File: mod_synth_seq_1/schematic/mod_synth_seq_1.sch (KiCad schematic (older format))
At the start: 43 parts, among them J1 CV1, J10 Reset, J11 Clock, J12 Gate Out, J2 Step 1 Gate, J3 Step 2 Gate, J4 Step 3 Gate, J5 Step 4 Gate

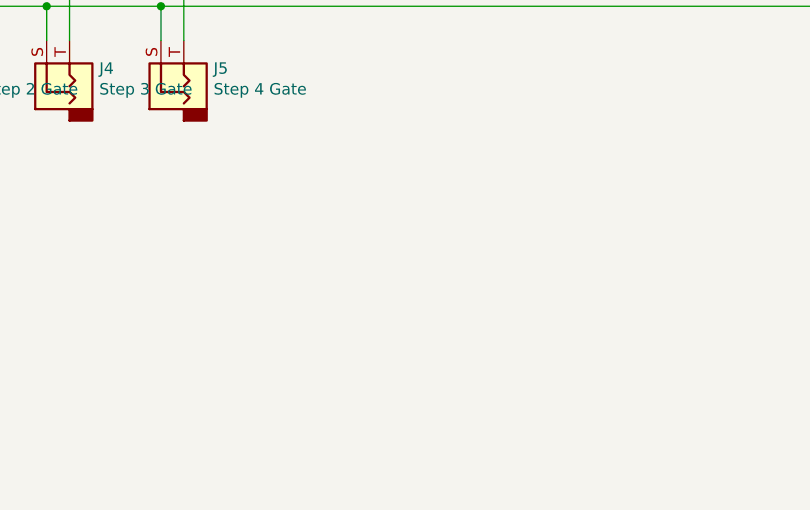
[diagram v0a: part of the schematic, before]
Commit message: Add missing connector
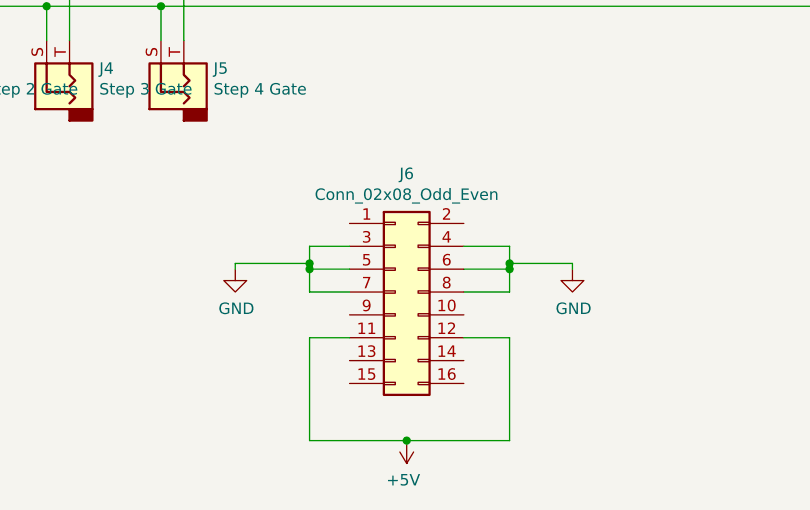
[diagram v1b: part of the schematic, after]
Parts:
- added J6: Conn_02x08_Odd_Even, Connector_IDC:IDC-Header_2x08_P2.54mm_Vertical, symbol Connector_Generic:Conn_02x08_Odd_Even
- R2, R20, R21, R4, R6, R8: footprint Resistor_THT:R_Axial_DIN0207_L6.3mm_D2.5mm_P10.16mm_Horizontal -> Resistor_THT:R_Axial_DIN0207_L6.3mm_D2.5mm_P2.54mm_Vertical
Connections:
- net +5V: now also J6.11 (Pin_11), J6.12 (Pin_12)
- net GND: now also J6.3 (Pin_3), J6.4 (Pin_4), J6.5 (Pin_5), J6.6 (Pin_6), J6.7 (Pin_7), J6.8 (Pin_8)
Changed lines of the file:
@@
 EESchema Schematic File Version 4
+LIBS:mod_synth_seq_1-cache
 EELAYER 29 0
 EELAYER END
@@
 F 0 "R2" H 2770 1546 50  0000 L CNN
 F 1 "1k" H 2770 1455 50  0000 L CNN
-F 2 "Resistor_THT:R_Axial_DIN0207_L6.3mm_D2.5mm_P10.16mm_Horizontal" V 2630 1500 50  0001 C CNN
+F 2 "Resistor_THT:R_Axial_DIN0207_L6.3mm_D2.5mm_P2.54mm_Vertical" V 2630 1500 50  0001 C CNN
 F 3 "~" H 2700 1500 50  0001 C CNN
 	1    2700 1500
@@
 F 0 "R4" H 3270 1546 50  0000 L CNN
 F 1 "1k" H 3270 1455 50  0000 L CNN
-F 2 "Resistor_THT:R_Axial_DIN0207_L6.3mm_D2.5mm_P10.16mm_Horizontal" V 3130 1500 50  0001 C CNN
+F 2 "Resistor_THT:R_Axial_DIN0207_L6.3mm_D2.5mm_P2.54mm_Vertical" V 3130 1500 50  0001 C CNN
 F 3 "~" H 3200 1500 50  0001 C CNN
 	1    3200 1500
@@
 F 0 "R6" H 3770 1546 50  0000 L CNN
 F 1 "1k" H 3770 1455 50  0000 L CNN
-F 2 "Resistor_THT:R_Axial_DIN0207_L6.3mm_D2.5mm_P10.16mm_Horizontal" V 3630 1500 50  0001 C CNN
+F 2 "Resistor_THT:R_Axial_DIN0207_L6.3mm_D2.5mm_P2.54mm_Vertical" V 3630 1500 50  0001 C CNN
 F 3 "~" H 3700 1500 50  0001 C CNN
 	1    3700 1500
@@
 F 0 "R8" H 4270 1546 50  0000 L CNN
 F 1 "1k" H 4270 1455 50  0000 L CNN
-F 2 "Resistor_THT:R_Axial_DIN0207_L6.3mm_D2.5mm_P10.16mm_Horizontal" V 4130 1500 50  0001 C CNN
+F 2 "Resistor_THT:R_Axial_DIN0207_L6.3mm_D2.5mm_P2.54mm_Vertical" V 4130 1500 50  0001 C CNN
 F 3 "~" H 4200 1500 50  0001 C CNN
 	1    4200 1500
@@
 F 0 "R20" H 9420 2796 50  0000 L CNN
 F 1 "1k" H 9420 2705 50  0000 L CNN
-F 2 "Resistor_THT:R_Axial_DIN0207_L6.3mm_D2.5mm_P10.16mm_Horizontal" V 9280 2750 50  0001 C CNN
+F 2 "Resistor_THT:R_Axial_DIN0207_L6.3mm_D2.5mm_P2.54mm_Vertical" V 9280 2750 50  0001 C CNN
 F 3 "~" H 9350 2750 50  0001 C CNN
 	1    9350 2750
@@
 F 0 "R21" H 9695 2796 50  0000 L CNN
 F 1 "1k" H 9695 2705 50  0000 L CNN
-F 2 "Resistor_THT:R_Axial_DIN0207_L6.3mm_D2.5mm_P10.16mm_Horizontal" V 9555 2750 50  0001 C CNN
+F 2 "Resistor_THT:R_Axial_DIN0207_L6.3mm_D2.5mm_P2.54mm_Vertical" V 9555 2750 50  0001 C CNN
 F 3 "~" H 9625 2750 50  0001 C CNN
 	1    9625 2750
@@
 Wire Wire Line
 	4250 5625 8800 5625
+$Comp
+L Connector_Generic:Conn_02x08_Odd_Even J6
+U 1 1 5D532A9C
+P 5275 6875
+F 0 "J6" H 5325 7392 50  0000 C CNN
+F 1 "Conn_02x08_Odd_Even" H 5325 7301 50  0000 C CNN
+F 2 "Connector_IDC:IDC-Header_2x08_P2.54mm_Vertical" H 5275 6875 50  0001 C CNN
+F 3 "~" H 5275 6875 50  0001 C CNN
+	1    5275 6875
+	1    0    0    -1
+$EndComp
+$Comp
+L power:GND #PWR0101
+U 1 1 5D5342E6
+P 6050 6775
+F 0 "#PWR0101" H 6050 6525 50  0001 C CNN
+F 1 "GND" H 6055 6602 50  0000 C CNN
+F 2 "" H 6050 6775 50  0001 C CNN
+F 3 "" H 6050 6775 50  0001 C CNN
+	1    6050 6775
+	1    0    0    -1
+$EndComp
+$Comp
+L power:GND #PWR0102
+U 1 1 5D5348F5
+P 4575 6775
+F 0 "#PWR0102" H 4575 6525 50  0001 C CNN
+F 1 "GND" H 4580 6602 50  0000 C CNN
+F 2 "" H 4575 6775 50  0001 C CNN
+F 3 "" H 4575 6775 50  0001 C CNN
+	1    4575 6775
+	1    0    0    -1
+$EndComp
+Wire Wire Line
+	5075 6675 4900 6675
+Wire Wire Line
+	4900 6675 4900 6750
+Wire Wire Line
+	4900 6775 5075 6775
+Wire Wire Line
+	5075 6875 4900 6875
+Wire Wire Line
+	4900 6875 4900 6775
+Connection ~ 4900 6775
+Wire Wire Line
+	4575 6750 4900 6750
+Wire Wire Line
+	4900 6750 4900 6775
+Connection ~ 4900 6750
+Wire Wire Line
+	4575 6775 4575 6750
+Wire Wire Line
+	5575 6675 5775 6675
+Wire Wire Line
+	5775 6675 5775 6750
+Wire Wire Line
+	5775 6875 5575 6875
+Wire Wire Line
+	5575 6775 5775 6775
+Connection ~ 5775 6775
+Wire Wire Line
+	5775 6775 5775 6875
+Wire Wire Line
+	5775 6750 6050 6750
+Wire Wire Line
+	6050 6750 6050 6775
+Connection ~ 5775 6750
+Wire Wire Line
+	5775 6750 5775 6775
+$Comp
+L power:+5V #PWR?
+U 1 1 5D58EE85
+P 5325 7525
+F 0 "#PWR?" H 5325 7375 50  0001 C CNN
+F 1 "+5V" H 5340 7698 50  0000 C CNN
+F 2 "" H 5325 7525 50  0001 C CNN
+F 3 "" H 5325 7525 50  0001 C CNN
+	1    5325 7525
+	-1   0    0    1
+$EndComp
+Wire Wire Line
+	5575 7075 5775 7075
+Wire Wire Line
+	5775 7075 5775 7525
+Wire Wire Line
+	5775 7525 5325 7525
+Wire Wire Line
+	5325 7525 4900 7525
+Wire Wire Line
+	4900 7525 4900 7075
+Wire Wire Line
+	4900 7075 5075 7075
+Connection ~ 5325 7525
 $EndSCHEMATC

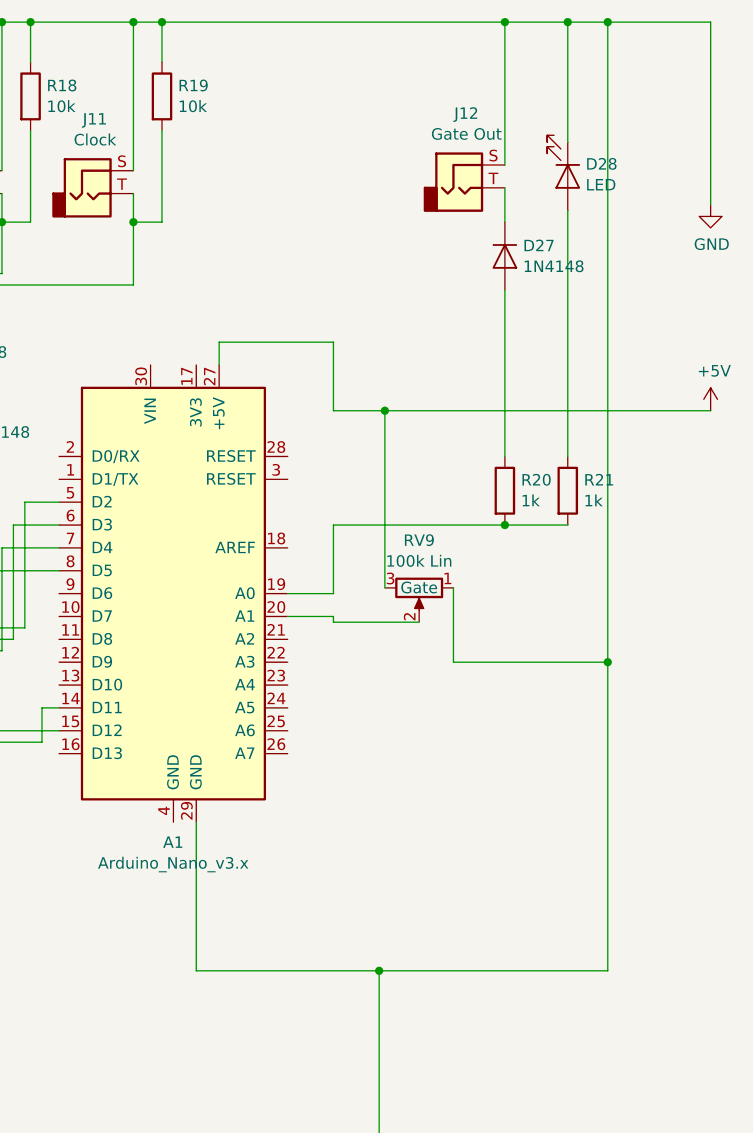
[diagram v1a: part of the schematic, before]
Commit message: Remove gate from smaller sequencer
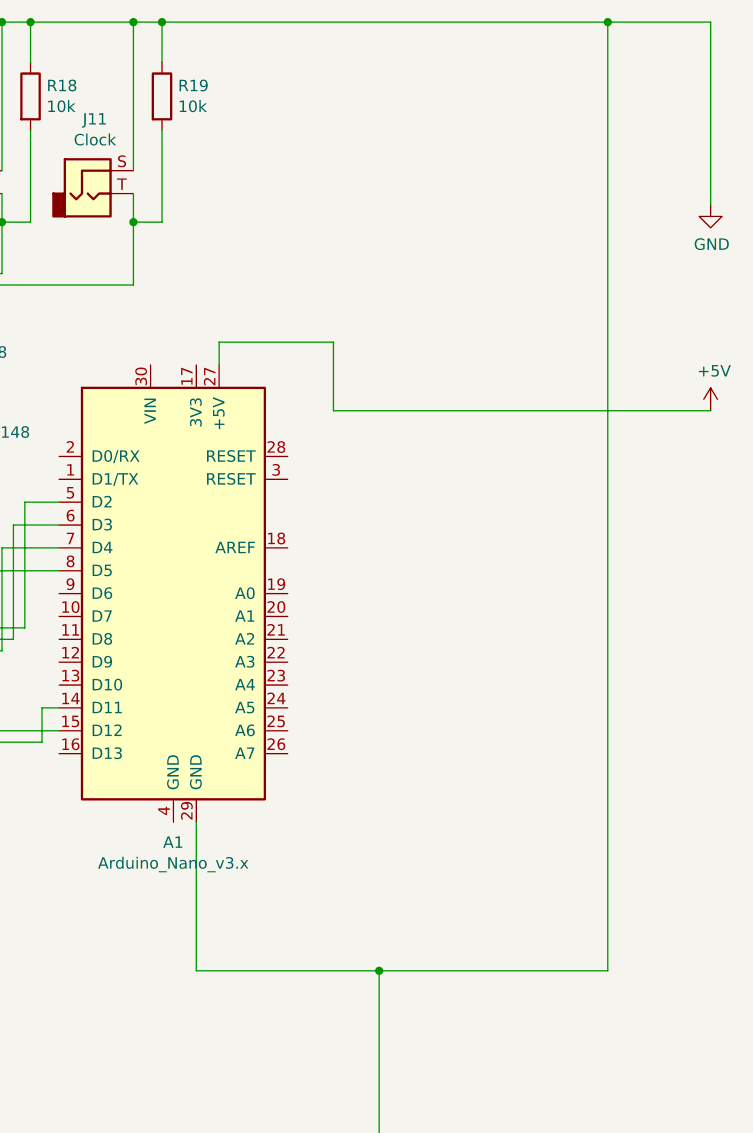
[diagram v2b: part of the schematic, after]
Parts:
- removed D27: 1N4148, Diode_THT:D_DO-35_SOD27_P7.62mm_Horizontal, symbol Diode:1N4148
- removed D28: LED, LED_THT:LED_D5.0mm, symbol Device:LED
- removed J12: Gate Out, Connector_Audio:Jack_3.5mm_QingPu_WQP-PJ398SM_Vertical_CircularHoles, symbol Connector:AudioJack2
- removed R20, R21: 1k, Resistor_THT:R_Axial_DIN0207_L6.3mm_D2.5mm_P2.54mm_Vertical, symbol Device:R
- removed RV9: 100k Lin, Potentiometer_THT:Potentiometer_Alpha_RD901F-40-00D_Single_Vertical, symbol Device:R_POT
- R2, R4, R6, R8: footprint Resistor_THT:R_Axial_DIN0207_L6.3mm_D2.5mm_P2.54mm_Vertical -> Resistor_THT:R_Axial_DIN0207_L6.3mm_D2.5mm_P10.16mm_Horizontal
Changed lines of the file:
@@
 Wire Wire Line
 	8000 4850 8800 4850
-Wire Wire Line
-	9800 4850 9800 3500
 Connection ~ 9800 700
-Wire Wire Line
-	9800 700  9625 700
 $Comp
 L Device:R R2
@@
 F 0 "R2" H 2770 1546 50  0000 L CNN
 F 1 "1k" H 2770 1455 50  0000 L CNN
-F 2 "Resistor_THT:R_Axial_DIN0207_L6.3mm_D2.5mm_P2.54mm_Vertical" V 2630 1500 50  0001 C CNN
+F 2 "Resistor_THT:R_Axial_DIN0207_L6.3mm_D2.5mm_P10.16mm_Horizontal" V 2630 1500 50  0001 C CNN
 F 3 "~" H 2700 1500 50  0001 C CNN
 	1    2700 1500
@@
 F 0 "R4" H 3270 1546 50  0000 L CNN
 F 1 "1k" H 3270 1455 50  0000 L CNN
-F 2 "Resistor_THT:R_Axial_DIN0207_L6.3mm_D2.5mm_P2.54mm_Vertical" V 3130 1500 50  0001 C CNN
+F 2 "Resistor_THT:R_Axial_DIN0207_L6.3mm_D2.5mm_P10.16mm_Horizontal" V 3130 1500 50  0001 C CNN
 F 3 "~" H 3200 1500 50  0001 C CNN
 	1    3200 1500
@@
 F 0 "R6" H 3770 1546 50  0000 L CNN
 F 1 "1k" H 3770 1455 50  0000 L CNN
-F 2 "Resistor_THT:R_Axial_DIN0207_L6.3mm_D2.5mm_P2.54mm_Vertical" V 3630 1500 50  0001 C CNN
+F 2 "Resistor_THT:R_Axial_DIN0207_L6.3mm_D2.5mm_P10.16mm_Horizontal" V 3630 1500 50  0001 C CNN
 F 3 "~" H 3700 1500 50  0001 C CNN
 	1    3700 1500
@@
 F 0 "R8" H 4270 1546 50  0000 L CNN
 F 1 "1k" H 4270 1455 50  0000 L CNN
-F 2 "Resistor_THT:R_Axial_DIN0207_L6.3mm_D2.5mm_P2.54mm_Vertical" V 4130 1500 50  0001 C CNN
+F 2 "Resistor_THT:R_Axial_DIN0207_L6.3mm_D2.5mm_P10.16mm_Horizontal" V 4130 1500 50  0001 C CNN
 F 3 "~" H 4200 1500 50  0001 C CNN
 	1    4200 1500
@@
 $EndComp
 Wire Wire Line
-	10250 2400 8825 2400
-Wire Wire Line
 	8600 2400 8600 2100
 Wire Wire Line
@@
 $EndComp
 $Comp
-L Connector:AudioJack2 J12
-U 1 1 5D1F520B
-P 9150 1425
-F 0 "J12" H 9182 1750 50  0000 C CNN
-F 1 "Gate Out" H 9182 1659 50  0000 C CNN
-F 2 "Connector_Audio:Jack_3.5mm_QingPu_WQP-PJ398SM_Vertical_CircularHoles" H 9150 1425 50  0001 C CNN
-F 3 "~" H 9150 1425 50  0001 C CNN
-	1    9150 1425
-	1    0    0    -1
-$EndComp
-$Comp
-L Device:R_POT RV9
-U 1 1 5D1F55B3
-P 8975 3175
-F 0 "RV9" V 8768 3175 50  0000 C CNN
-F 1 "100k Lin" V 8859 3175 50  0000 C CNN
-F 2 "Potentiometer_THT:Potentiometer_Alpha_RD901F-40-00D_Single_Vertical" H 8975 3175 50  0001 C CNN
-F 3 "~" H 8975 3175 50  0001 C CNN
-F 4 "Gate" V 8975 3175 50  0000 C CNN "Text"
-	1    8975 3175
-	0    1    1    0
-$EndComp
-$Comp
 L Connector:AudioJack2 J2
 U 1 1 5D1F5CD9
@@
 $EndComp
 $Comp
-L Device:R R20
-U 1 1 5D1835EC
-P 9350 2750
-F 0 "R20" H 9420 2796 50  0000 L CNN
-F 1 "1k" H 9420 2705 50  0000 L CNN
-F 2 "Resistor_THT:R_Axial_DIN0207_L6.3mm_D2.5mm_P2.54mm_Vertical" V 9280 2750 50  0001 C CNN
-F 3 "~" H 9350 2750 50  0001 C CNN
-	1    9350 2750
-	1    0    0    -1
-$EndComp
-$Comp
 L Device:R R5
 U 1 1 5D183849
@@
 Wire Wire Line
 	6925 1850 6925 2300
-Wire Wire Line
-	8600 2900 8600 3200
-Wire Wire Line
-	8600 3200 8400 3200
-Wire Wire Line
-	9350 1425 9350 1575
-$Comp
-L Diode:1N4148 D27
-U 1 1 5D291621
-P 9350 1725
-F 0 "D27" V 9304 1804 50  0000 L CNN
-F 1 "1N4148" V 9395 1804 50  0000 L CNN
-F 2 "Diode_THT:D_DO-35_SOD27_P7.62mm_Horizontal" H 9350 1550 50  0001 C CNN
-F 3 "https://assets.nexperia.com/documents/data-sheet/1N4148_1N4448.pdf" H 9350 1725 50  0001 C CNN
-	1    9350 1725
-	0    1    1    0
-$EndComp
-Wire Wire Line
-	9350 1875 9350 2600
 $Comp
 L Diode:1N4148 D25
@@
 	6925 1850 7725 1850
 Wire Wire Line
-	9350 1325 9350 700
-Connection ~ 9350 700
-Wire Wire Line
-	9350 700  7850 700
-Wire Wire Line
 	7725 1350 7725 700
 Connection ~ 7725 700
@@
 	7725 1575 7725 1850
 Wire Wire Line
-	8975 3325 8600 3325
-Wire Wire Line
-	8600 3325 8600 3300
-Wire Wire Line
-	8600 3300 8400 3300
-Wire Wire Line
-	8825 3175 8825 2400
-Connection ~ 8825 2400
-Wire Wire Line
-	8825 2400 8600 2400
-Wire Wire Line
-	9125 3175 9125 3500
-Wire Wire Line
-	9125 3500 9800 3500
-Connection ~ 9800 3500
-Wire Wire Line
 	1550 2550 1800 2550
 Wire Wire Line
@@
 	4250 5775 4250 5625
 Connection ~ 4250 5625
-Wire Wire Line
-	9800 700  9800 3500
 Connection ~ 4275 3500
 Wire Wire Line
@@
 Wire Wire Line
 	4500 700  4500 2100
-$Comp
-L Device:LED D28
-U 1 1 5D6A7AA8
-P 9625 1375
-F 0 "D28" V 9572 1453 50  0000 L CNN
-F 1 "LED" V 9663 1453 50  0000 L CNN
-F 2 "LED_THT:LED_D5.0mm" H 9625 1375 50  0001 C CNN
-F 3 "~" H 9625 1375 50  0001 C CNN
-	1    9625 1375
-	0    1    1    0
-$EndComp
-Wire Wire Line
-	9625 1225 9625 700
-Connection ~ 9625 700
-Wire Wire Line
-	9625 700  9350 700
-$Comp
-L Device:R R21
-U 1 1 5D6B54FD
-P 9625 2750
-F 0 "R21" H 9695 2796 50  0000 L CNN
-F 1 "1k" H 9695 2705 50  0000 L CNN
-F 2 "Resistor_THT:R_Axial_DIN0207_L6.3mm_D2.5mm_P2.54mm_Vertical" V 9555 2750 50  0001 C CNN
-F 3 "~" H 9625 2750 50  0001 C CNN
-	1    9625 2750
-	1    0    0    -1
-$EndComp
-Wire Wire Line
-	8600 2900 9350 2900
-Connection ~ 9350 2900
-Wire Wire Line
-	9350 2900 9625 2900
-Wire Wire Line
-	9625 2600 9625 1525
 Wire Wire Line
 	4500 700  7150 700
@@
 	5775 6750 5775 6775
 $Comp
-L power:+5V #PWR?
+L power:+5V #PWR0103
 U 1 1 5D58EE85
 P 5325 7525
-F 0 "#PWR?" H 5325 7375 50  0001 C CNN
+F 0 "#PWR0103" H 5325 7375 50  0001 C CNN
 F 1 "+5V" H 5340 7698 50  0000 C CNN
 F 2 "" H 5325 7525 50  0001 C CNN
@@
 	4900 7075 5075 7075
 Connection ~ 5325 7525
+Wire Wire Line
+	7850 700  9800 700
+Wire Wire Line
+	8600 2400 10250 2400
+Wire Wire Line
+	9800 700  9800 4850
 $EndSCHEMATC

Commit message: Change potentiometer pads
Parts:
- RV1, RV2, RV3, RV4: footprint Potentiometer_THT:Potentiometer_Alpha_RD901F-40-00D_Single_Vertical -> Potentiometer_THT:Potentiometer_Alpha_RD901F-40-00D_Single_Vertical_CircularHoles
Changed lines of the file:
@@
 F 0 "RV1" V 2643 2100 50  0000 C CNN
 F 1 "100k Lin" V 2734 2100 50  0000 C CNN
-F 2 "Potentiometer_THT:Potentiometer_Alpha_RD901F-40-00D_Single_Vertical" H 2850 2100 50  0001 C CNN
+F 2 "Potentiometer_THT:Potentiometer_Alpha_RD901F-40-00D_Single_Vertical_CircularHoles" H 2850 2100 50  0001 C CNN
 F 3 "~" H 2850 2100 50  0001 C CNN
 	1    2850 2100
@@
 F 0 "RV2" V 3143 2100 50  0000 C CNN
 F 1 "100k Lin" V 3234 2100 50  0000 C CNN
-F 2 "Potentiometer_THT:Potentiometer_Alpha_RD901F-40-00D_Single_Vertical" H 3350 2100 50  0001 C CNN
+F 2 "Potentiometer_THT:Potentiometer_Alpha_RD901F-40-00D_Single_Vertical_CircularHoles" H 3350 2100 50  0001 C CNN
 F 3 "~" H 3350 2100 50  0001 C CNN
 	1    3350 2100
@@
 F 0 "RV3" V 3643 2100 50  0000 C CNN
 F 1 "100k Lin" V 3734 2100 50  0000 C CNN
-F 2 "Potentiometer_THT:Potentiometer_Alpha_RD901F-40-00D_Single_Vertical" H 3850 2100 50  0001 C CNN
+F 2 "Potentiometer_THT:Potentiometer_Alpha_RD901F-40-00D_Single_Vertical_CircularHoles" H 3850 2100 50  0001 C CNN
 F 3 "~" H 3850 2100 50  0001 C CNN
 	1    3850 2100
@@
 F 0 "RV4" V 4143 2100 50  0000 C CNN
 F 1 "100k Lin" V 4234 2100 50  0000 C CNN
-F 2 "Potentiometer_THT:Potentiometer_Alpha_RD901F-40-00D_Single_Vertical" H 4350 2100 50  0001 C CNN
+F 2 "Potentiometer_THT:Potentiometer_Alpha_RD901F-40-00D_Single_Vertical_CircularHoles" H 4350 2100 50  0001 C CNN
 F 3 "~" H 4350 2100 50  0001 C CNN
 	1    4350 2100
